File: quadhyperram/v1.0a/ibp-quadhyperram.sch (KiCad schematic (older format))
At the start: 2 parts, among them J2 PMOD, J4 PMOD

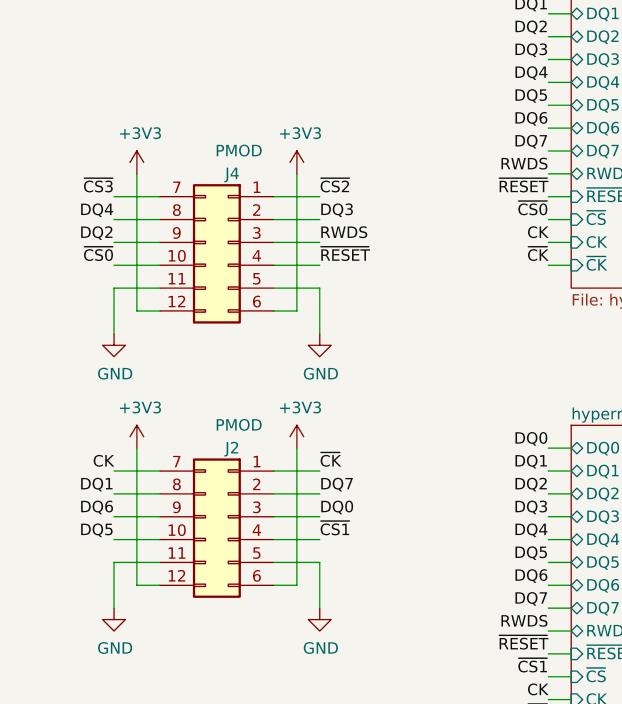
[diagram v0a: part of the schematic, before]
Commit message: Updated quadhyperram Pmod with length matched signals.
Only data, RWDS and Clock signals are length matched. CS is not that
critical and RESET is totally timing irrelevant as far as I know.
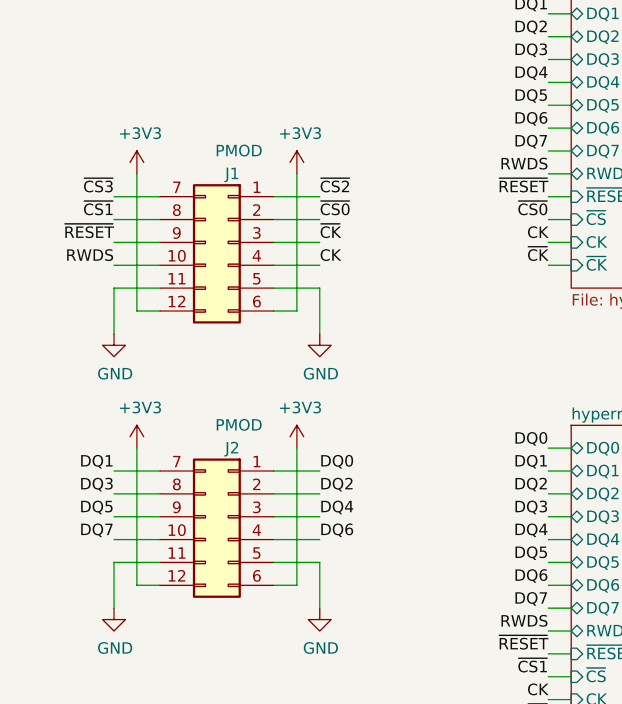
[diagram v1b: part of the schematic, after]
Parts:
- renumbered J4 to J1
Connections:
- net CK: now also J1.4 (Pin_4); no longer J2.7 (Pin_7)
- net DQ0: now also J2.1 (Pin_1); no longer J2.3 (Pin_3)
- net DQ1: now also J2.7 (Pin_7); no longer J2.8 (Pin_8)
- net DQ2: now also J2.2 (Pin_2); no longer J1.9 (Pin_9)
- net DQ3: now also J2.8 (Pin_8); no longer J1.2 (Pin_2)
- net DQ4: now also J2.3 (Pin_3); no longer J1.8 (Pin_8)
- net DQ5: now also J2.9 (Pin_9); no longer J2.10 (Pin_10)
- net DQ6: now also J2.4 (Pin_4); no longer J2.9 (Pin_9)
- net DQ7: now also J2.10 (Pin_10); no longer J2.2 (Pin_2)
- net RWDS: now also J1.10 (Pin_10); no longer J1.3 (Pin_3)
- net ~CK: now also J1.3 (Pin_3); no longer J2.1 (Pin_1)
- net ~CS0: now also J1.2 (Pin_2); no longer J1.10 (Pin_10)
- net ~CS1: now also J1.8 (Pin_8); no longer J2.4 (Pin_4)
- net ~RESET: now also J1.9 (Pin_9); no longer J1.4 (Pin_4)
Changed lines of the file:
@@
 $EndDescr
 $Comp
-L Connector_Generic:Conn_02x06_Top_Bottom J4
+L Connector_Generic:Conn_02x06_Top_Bottom J1
 U 1 1 5AB98614
 P 2000 3300
-F 0 "J4" H 1950 3600 50  0000 L CNN
+F 0 "J1" H 1950 3600 50  0000 L CNN
 F 1 "PMOD" H 1850 3700 50  0000 L CNN
 F 2 "pkl_connectors:PMODHeader_2x06_P2.54mm_Horizontal" H 2000 3300 50  0001 C CNN
@@
 	1    0    0    -1
 $EndComp
+Text Label 1500 4500 2    50   ~ 0
+DQ5
+Text Label 2400 4300 0    50   ~ 0
+DQ0
+Text Label 2400 4600 0    50   ~ 0
+DQ6
 Text Label 1500 4600 2    50   ~ 0
-DQ5
+DQ7
+Text Label 1500 4300 2    50   ~ 0
+DQ1
+Text Label 2400 3300 0    50   ~ 0
+~CK
+Text Label 2400 3400 0    50   ~ 0
+CK
+Text Label 1500 3300 2    50   ~ 0
+~RESET
+Text Label 2400 3200 0    50   ~ 0
+~CS0
+Text Label 1500 3400 2    50   ~ 0
+RWDS
+Text Label 2400 4400 0    50   ~ 0
+DQ2
+Text Label 1500 4400 2    50   ~ 0
+DQ3
 Text Label 2400 4500 0    50   ~ 0
-DQ0
-Text Label 1500 4500 2    50   ~ 0
-DQ6
-Text Label 2400 4400 0    50   ~ 0
-DQ7
-Text Label 1500 4400 2    50   ~ 0
-DQ1
-Text Label 2400 4300 0    50   ~ 0
-~CK
-Text Label 1500 4300 2    50   ~ 0
-CK
-Text Label 2400 3400 0    50   ~ 0
-~RESET
-Text Label 1500 3400 2    50   ~ 0
-~CS0
-Text Label 2400 3300 0    50   ~ 0
-RWDS
-Text Label 1500 3300 2    50   ~ 0
-DQ2
-Text Label 2400 3200 0    50   ~ 0
-DQ3
-Text Label 1500 3200 2    50   ~ 0
 DQ4
 Wire Wire Line
@@
 Text Label 3400 3400 2    50   ~ 0
 ~CK
-Text Label 2400 4600 0    50   ~ 0
+Text Label 1500 3200 2    50   ~ 0
 ~CS1
 Wire Wire Line

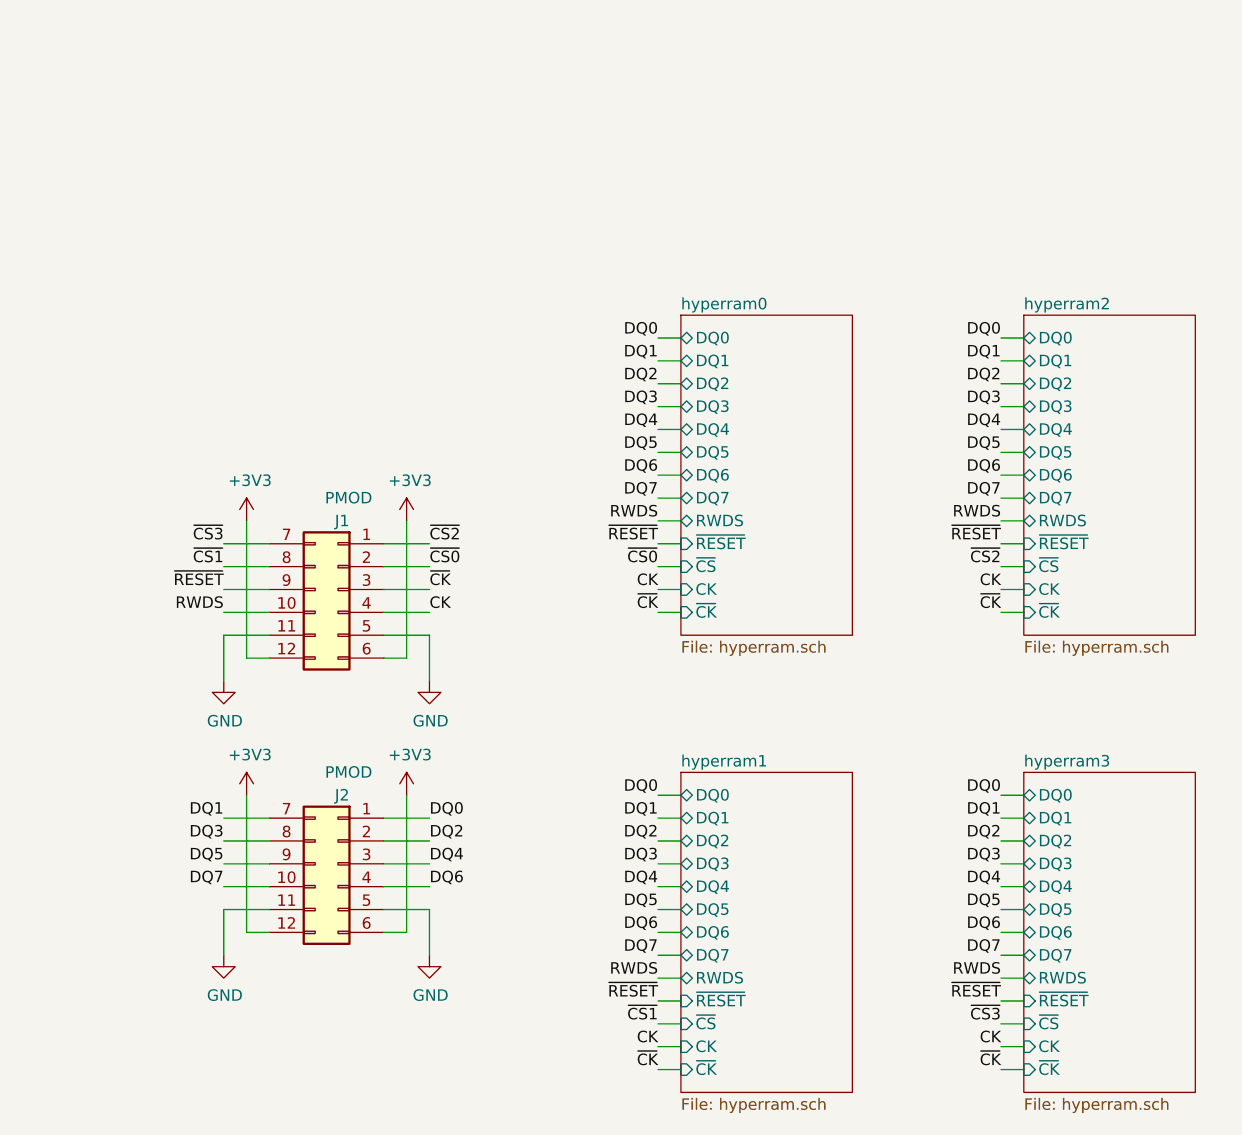
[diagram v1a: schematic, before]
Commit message: Added optional 1v8 vreg for higher speed S27KS chips.
When using the S27KS chips, the host Pmod IO voltage has to be set to
1.8V too. But as it often is bit of a hassle to change the supply
voltage on the Pmod connector we provide the option of mounting a 1.8V
regulator directly on the Pmod itself to power the chips.
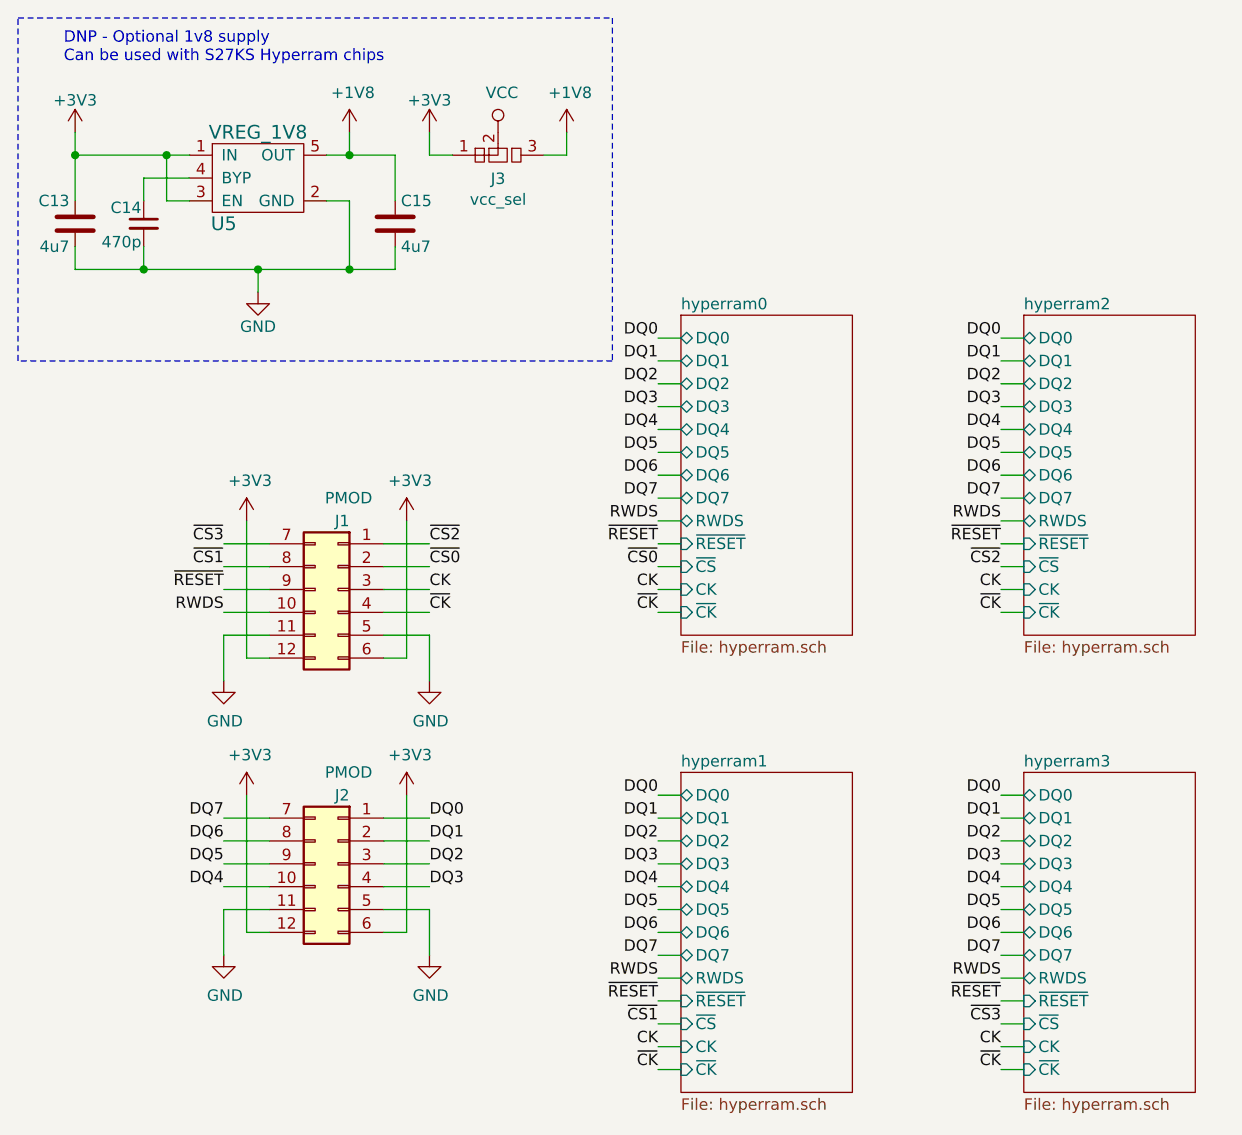
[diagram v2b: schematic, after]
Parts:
- added C13, C15: 4u7, pkl_dipol:C_0603, symbol pkl_device:pkl_C
- added C14: 470p, pkl_dipol:C_0402, symbol pkl_device:pkl_C_Small
- added J3: vcc_sel, pkl_jumpers:J_NCNO_0903_30, symbol pkl_misc:pkl_double_jumper_ncno
- added U5: VREG_1V8, pkl_housings_sot:SOT-23-5, symbol pkl_device:pkl_VREG_5PIN_FIXED
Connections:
- net +3V3: now also C13.1, J3.1, U5.1 (IN), U5.3 (EN)
- net CK: now also J1.3 (Pin_3); no longer J1.4 (Pin_4)
- net DQ1: now also J2.2 (Pin_2); no longer J2.7 (Pin_7)
- net DQ2: now also J2.3 (Pin_3); no longer J2.2 (Pin_2)
- net DQ3: now also J2.4 (Pin_4); no longer J2.8 (Pin_8)
- net DQ4: now also J2.10 (Pin_10); no longer J2.3 (Pin_3)
- net DQ6: now also J2.8 (Pin_8); no longer J2.4 (Pin_4)
- net DQ7: now also J2.7 (Pin_7); no longer J2.10 (Pin_10)
- net GND: now also C13.2, C14.2, C15.2, U5.2 (GND)
- net ~CK: now also J1.4 (Pin_4); no longer J1.3 (Pin_3)
- new net: C14.1, U5.4 (BYP)
- new net +1V8: C15.1, J3.3, U5.5 (OUT)
- new net VCC: J3.2
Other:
- note added: "DNP - Optional 1v8 supply\nCan be used with S27KS Hyperram chips"
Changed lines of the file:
@@
 Text Label 2400 4300 0    50   ~ 0
 DQ0
-Text Label 2400 4600 0    50   ~ 0
+Text Label 1500 4400 2    50   ~ 0
 DQ6
-Text Label 1500 4600 2    50   ~ 0
+Text Label 1500 4300 2    50   ~ 0
 DQ7
-Text Label 1500 4300 2    50   ~ 0
+Text Label 2400 4400 0    50   ~ 0
 DQ1
+Text Label 2400 3400 0    50   ~ 0
+~CK
 Text Label 2400 3300 0    50   ~ 0
-~CK
-Text Label 2400 3400 0    50   ~ 0
 CK
 Text Label 1500 3300 2    50   ~ 0
@@
 Text Label 1500 3400 2    50   ~ 0
 RWDS
-Text Label 2400 4400 0    50   ~ 0
+Text Label 2400 4500 0    50   ~ 0
 DQ2
-Text Label 1500 4400 2    50   ~ 0
+Text Label 2400 4600 0    50   ~ 0
 DQ3
-Text Label 2400 4500 0    50   ~ 0
+Text Label 1500 4600 2    50   ~ 0
 DQ4
 Wire Wire Line
@@
 Text Label 4900 5400 2    50   ~ 0
 ~CK
+$Comp
+L pkl_device:pkl_C C13
+U 1 1 5E178F91
+P 850 1700
+F 0 "C13" H 875 1800 50  0000 L CNN
+F 1 "4u7" H 875 1600 50  0000 L CNN
+F 2 "pkl_dipol:C_0603" H 888 1550 30  0001 C CNN
+F 3 "" H 850 1700 60  0000 C CNN
+F 4 "cap-cer-0603-4u7" H 850 1700 60  0001 C CNN "Key"
+F 5 "0603" H 850 1700 60  0001 C CNN "Package ID"
+F 6 "ANY" H 850 1700 60  0001 C CNN "Source"
+F 7 "DNP" H 850 1700 50  0001 C CNN "DNP"
+	1    850  1700
+	-1   0    0    -1
+$EndComp
+$Comp
+L pkl_device:pkl_VREG_5PIN_FIXED U5
+U 1 1 5E178F9C
+P 1650 1500
+F 0 "U5" H 1500 1300 60  0000 C CNN
+F 1 "VREG_1V8" H 1650 1700 60  0000 C CNN
+F 2 "pkl_housings_sot:SOT-23-5" H 1650 1500 60  0001 C CNN
+F 3 "https://www.maxlinear.com/ds/spx3819.pdf" H 1650 1500 60  0001 C CNN
+F 4 "vreg-sot23-5-1v8" H 1650 1500 60  0001 C CNN "Key"
+F 5 "sot23-5" H 1650 1500 60  0001 C CNN "Package ID"
+F 6 "ANY" H 1650 1500 60  0001 C CNN "Source"
+F 7 "DNP" H 1650 1500 50  0001 C CNN "DNP"
+F 8 "Exar" H 1650 1500 50  0001 C CNN "Manufacturer"
+F 9 "SPX3819M5-L-1-8/TR" H 1650 1500 50  0001 C CNN "MFN"
+	1    1650 1500
+	1    0    0    -1
+$EndComp
+$Comp
+L pkl_device:pkl_C C15
+U 1 1 5E178FA6
+P 2250 1700
+F 0 "C15" H 2275 1800 50  0000 L CNN
+F 1 "4u7" H 2275 1600 50  0000 L CNN
+F 2 "pkl_dipol:C_0603" H 2288 1550 30  0001 C CNN
+F 3 "" H 2250 1700 60  0000 C CNN
+F 4 "cap-cer-0603-4u7" H 2250 1700 60  0001 C CNN "Key"
+F 5 "0603" H 2250 1700 60  0001 C CNN "Package ID"
+F 6 "ANY" H 2250 1700 60  0001 C CNN "Source"
+F 7 "DNP" H 2250 1700 50  0001 C CNN "DNP"
+	1    2250 1700
+	1    0    0    -1
+$EndComp
+$Comp
+L power:GND #PWR0109
+U 1 1 5E178FAD
+P 1650 2000
+F 0 "#PWR0109" H 1650 1750 50  0001 C CNN
+F 1 "GND" H 1650 1850 50  0000 C CNN
+F 2 "" H 1650 2000 60  0000 C CNN
+F 3 "" H 1650 2000 60  0000 C CNN
+F 4 "ANY" H 1650 2000 50  0001 C CNN "Source"
+	1    1650 2000
+	1    0    0    -1
+$EndComp
+$Comp
+L pkl_device:pkl_C_Small C14
+U 1 1 5E178FB7
+P 1150 1700
+F 0 "C14" H 1160 1770 50  0000 L CNN
+F 1 "470p" H 1160 1620 50  0000 L CNN
+F 2 "pkl_dipol:C_0402" H 1150 1700 60  0001 C CNN
+F 3 "" H 1150 1700 60  0000 C CNN
+F 4 "cap-cer-0402-470p" H 1150 1700 60  0001 C CNN "Key"
+F 5 "0402" H 1150 1700 60  0001 C CNN "Package ID"
+F 6 "ANY" H 1150 1700 60  0001 C CNN "Source"
+F 7 "DNP" H 1150 1700 50  0001 C CNN "DNP"
+	1    1150 1700
+	-1   0    0    -1
+$EndComp
+$Comp
+L power:+3V3 #PWR0110
+U 1 1 5E178FBE
+P 850 1300
+F 0 "#PWR0110" H 850 1150 50  0001 C CNN
+F 1 "+3V3" H 850 1440 50  0000 C CNN
+F 2 "" H 850 1300 60  0000 C CNN
+F 3 "" H 850 1300 60  0000 C CNN
+F 4 "ANY" H 850 1300 50  0001 C CNN "Source"
+	1    850  1300
+	1    0    0    -1
+$EndComp
+Wire Wire Line
+	850  1400 1250 1400
+Wire Wire Line
+	1250 1400 1350 1400
+Wire Wire Line
+	1250 1400 1250 1600
+Wire Wire Line
+	1250 1600 1350 1600
+Connection ~ 1250 1400
+Wire Wire Line
+	1950 1600 2050 1600
+Wire Wire Line
+	2050 1900 2050 1600
+Wire Wire Line
+	850  1900 1150 1900
+Wire Wire Line
+	1150 1900 1650 1900
+Wire Wire Line
+	1650 1900 2050 1900
+Wire Wire Line
+	2050 1900 2250 1900
+Wire Wire Line
+	1650 1900 1650 2000
+Wire Wire Line
+	850  1900 850  1800
+Connection ~ 1650 1900
+Wire Wire Line
+	1350 1500 1150 1500
+Wire Wire Line
+	1150 1500 1150 1600
+Wire Wire Line
+	1150 1800 1150 1900
+Connection ~ 1150 1900
+Wire Wire Line
+	850  1300 850  1400
+Wire Wire Line
+	850  1400 850  1600
+Wire Wire Line
+	1950 1400 2050 1400
+Wire Wire Line
+	2050 1400 2250 1400
+Wire Wire Line
+	2250 1400 2250 1600
+Wire Wire Line
+	2250 1900 2250 1800
+Connection ~ 2050 1900
+Wire Wire Line
+	2050 1300 2050 1400
+Connection ~ 2050 1400
+Connection ~ 850  1400
+Wire Notes Line
+	3200 2300 600  2300
+Wire Notes Line
+	600  2300 600  800
+Wire Notes Line
+	600  800  3200 800
+Wire Notes Line
+	3200 800  3200 2300
+Text Notes 800  1000 0    50   ~ 0
+DNP - Optional 1v8 supply\nCan be used with S27KS Hyperram chips
+$Comp
+L power:+1V8 #PWR0111
+U 1 1 5E16F7EA
+P 2050 1300
+F 0 "#PWR0111" H 2050 1150 50  0001 C CNN
+F 1 "+1V8" H 2065 1473 50  0000 C CNN
+F 2 "" H 2050 1300 50  0001 C CNN
+F 3 "" H 2050 1300 50  0001 C CNN
+	1    2050 1300
+	1    0    0    -1
+$EndComp
+$Comp
+L pkl_misc:pkl_double_jumper_ncno J3
+U 1 1 5E1962AE
+P 2700 1400
+F 0 "J3" H 2700 1297 50  0000 C CNN
+F 1 "vcc_sel" H 2700 1206 50  0000 C CNN
+F 2 "pkl_jumpers:J_NCNO_0903_30" H 2650 1400 50  0001 C CNN
+F 3 "" H 2650 1400 50  0001 C CNN
+	1    2700 1400
+	1    0    0    -1
+$EndComp
+$Comp
+L power:+1V8 #PWR0112
+U 1 1 5E19C151
+P 3000 1300
+F 0 "#PWR0112" H 3000 1150 50  0001 C CNN
+F 1 "+1V8" H 3015 1473 50  0000 C CNN
+F 2 "" H 3000 1300 50  0001 C CNN
+F 3 "" H 3000 1300 50  0001 C CNN
+	1    3000 1300
+	1    0    0    -1
+$EndComp
+$Comp
+L power:+3V3 #PWR0113
+U 1 1 5E19C6CD
+P 2400 1300
+F 0 "#PWR0113" H 2400 1150 50  0001 C CNN
+F 1 "+3V3" H 2400 1440 50  0000 C CNN
+F 2 "" H 2400 1300 60  0000 C CNN
+F 3 "" H 2400 1300 60  0000 C CNN
+F 4 "ANY" H 2400 1300 50  0001 C CNN "Source"
+	1    2400 1300
+	1    0    0    -1
+$EndComp
+$Comp
+L power:VCC #PWR0114
+U 1 1 5E1A1732
+P 2700 1300
+F 0 "#PWR0114" H 2700 1150 50  0001 C CNN
+F 1 "VCC" H 2717 1473 50  0000 C CNN
+F 2 "" H 2700 1300 50  0001 C CNN
+F 3 "" H 2700 1300 50  0001 C CNN
+	1    2700 1300
+	1    0    0    -1
+$EndComp
+Wire Wire Line
+	2900 1400 3000 1400
+Wire Wire Line
+	3000 1400 3000 1300
+Wire Wire Line
+	2400 1300 2400 1400
+Wire Wire Line
+	2400 1400 2500 1400
 $EndSCHEMATC
